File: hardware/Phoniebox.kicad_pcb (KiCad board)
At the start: 2 copper layers, 65 x 56.5 mm, 80 parts, among them J1 GPIO, J2 Screw_Terminal_01x08, J3 Screw_Terminal_01x08, J4 Screw_Terminal_01x08, J7 USB_B_Micro, J8 Conn_02x04_Odd_Even, Q1 2N7002, Q2 2N7002, Q3 2N7002, Q4 2N7002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

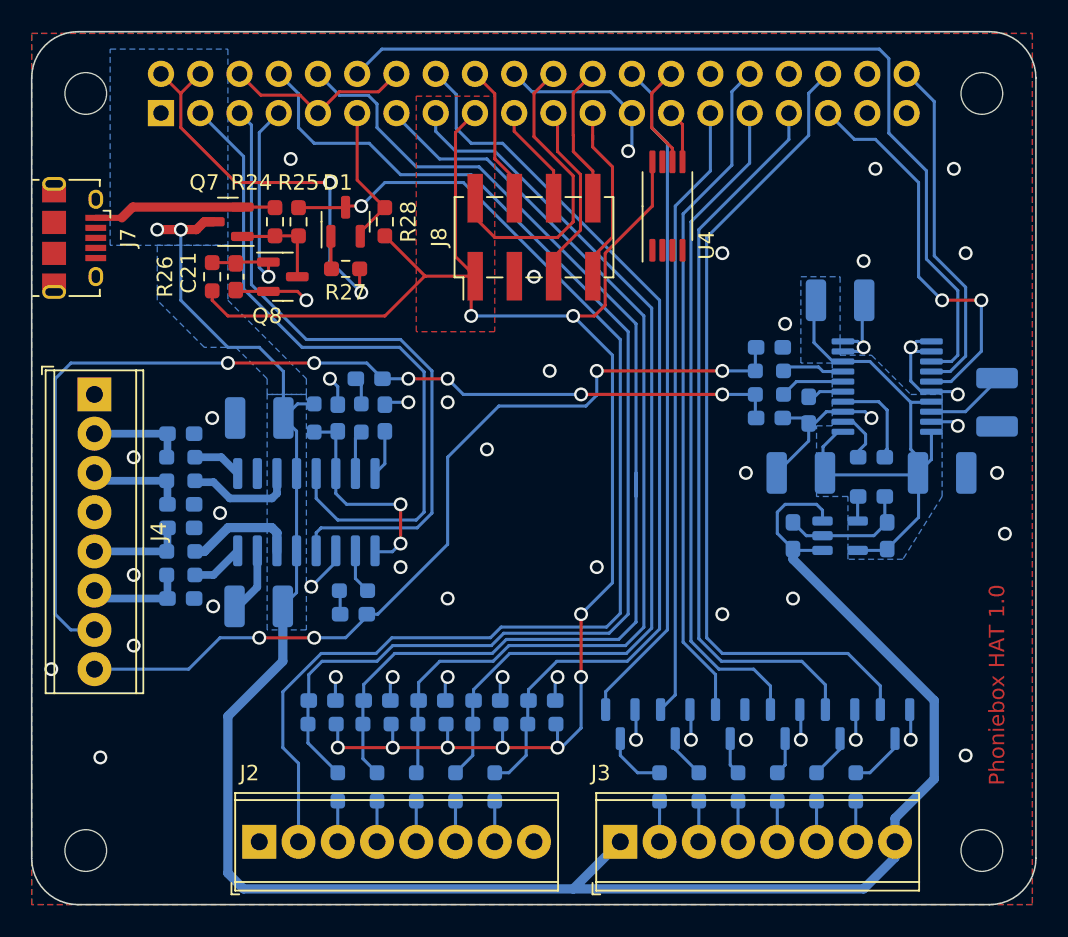
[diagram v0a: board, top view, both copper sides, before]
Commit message: Add I2C header for displays. Mute/SHDN now controlled by previously unused GPIO20/26. LED1 is now hardwired to ON=V3P3 high. GPIO7 would still be available to control LED1. Change debounce circuit to have both directions up/down debounced. Use resistor/capacitor values to debounce button press times <100ms.
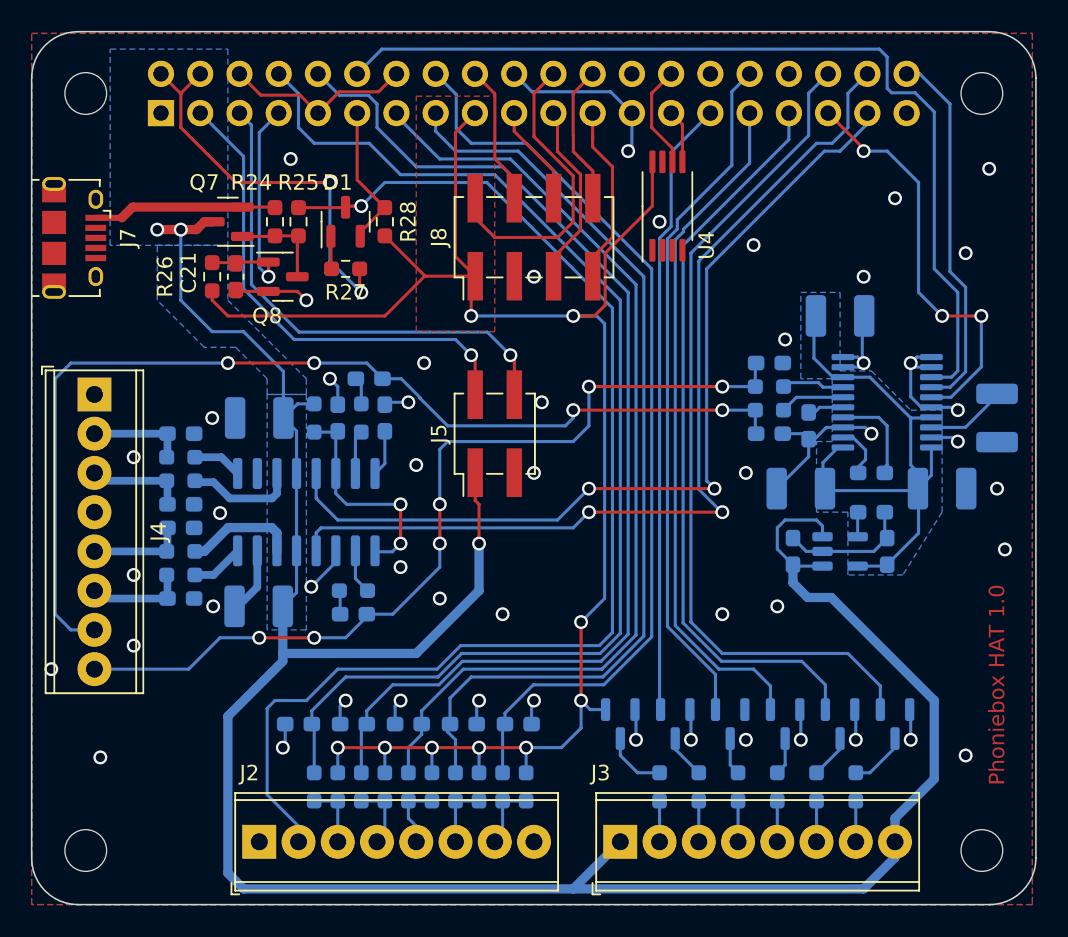
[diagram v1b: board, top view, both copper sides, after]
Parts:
- added J5: Conn_02x02_Odd_Even, Connector_PinHeader_2.54mm:PinHeader_2x02_P2.54mm_Vertical_SMD, F.Cu at (130.0, 69.5)
- C14, C15, C16, C8, C9: value 1n -> 1u
- R10, R12, R20, R6, R8: value 10k -> 33k
- R13, R21, R7, R9: value 100 -> 33k
- moved R20 4.19 mm to (132.0, 92.4), turned to 90 degrees
- moved R6 4.19 mm to (119.8, 92.4), turned to 90 degrees
- moved R12 4.10 mm to (129.0, 92.4), turned to 90 degrees
- moved R8 4.10 mm to (122.9, 92.4), turned to 90 degrees
- moved R10 4.06 mm to (125.9, 92.4), turned to 90 degrees
- moved C14 2.16 mm to (124.4, 88.3), turned to 180 degrees
- moved C15 2.16 mm to (127.9, 88.3)
- moved C16 2.16 mm to (131.5, 88.3)
- moved C8 2.16 mm to (117.3, 88.3), turned to 180 degrees
- moved C9 2.16 mm to (120.8, 88.3), turned to 180 degrees
- moved R7 1.52 mm to (118.3, 92.4)
- moved C17 1.02 mm to (149.3, 77.1)
- moved C22 1.02 mm to (155.4, 77.1)
- moved C24 1.02 mm to (154.4, 72.1)
- moved C25 1.02 mm to (150.3, 69.0)
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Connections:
- J1 pad 3: /GPIO2 -> /GPIO2_SDA
- J1 pad 37: /GPIO[26] -> /GPIO26
- J1 pad 38: /GPIO[20]/PCM.DIN -> /GPIO20
- J1 pad 5: /GPIO3 -> /GPIO3_SCL
- Q1 pad 1: /GPIO7 -> +3V3
- R10 pad 1: /GPIO27 -> /Button_4
- R12 pad 1: /GPIO22 -> /Button_5
- R20 pad 1: /GPIO23 -> /Button_6
- R6 pad 1: /GPIO14 -> /Button_2
- R8 pad 1: /GPIO15 -> /Button_3
- U1 pad 12: /GPIO3 -> /GPIO20
- U1 pad 5: /GPIO2 -> /GPIO26
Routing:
- net /GPIO20: track 0.00 -> 62.2 mm, vias 0 -> 2
- net /GPIO26: track 0.00 -> 58.2 mm, vias 0 -> 2
- net /GPIO2: track 44.9 -> 0.00 mm
- net /GPIO3: track 43.9 -> 0.00 mm
- net /GPIO7: track 43.8 -> 0.00 mm
- net /GPIO3_SCL: track 0.00 -> 32.7 mm, vias 0 -> 1
- net /GPIO2_SDA: track 0.00 -> 31.7 mm, vias 0 -> 1
- net +5V: track 162.8 -> 184.8 mm, vias 4 -> 5
- net +3V3: track 109.3 -> 111.9 mm
- net /GPIO15: track 74.4 -> 72.1 mm
- net /GPIO18: track 58.3 -> 60.2 mm
- net /Button_4: track 2.64 -> 4.38 mm
- net /Button_3: track 2.64 -> 4.38 mm
- net /Button_6: track 2.64 -> 4.38 mm
- net /Button_1: track 77.5 -> 79.2 mm
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
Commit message: Add BOM descriptions and JLC PCB LCSC part numbers. Generate gerber, drill and pick-and-place files.
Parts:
- C24, C25: value 2u2 -> 4u7
- U4: value CAT24C128 -> CAT24C32

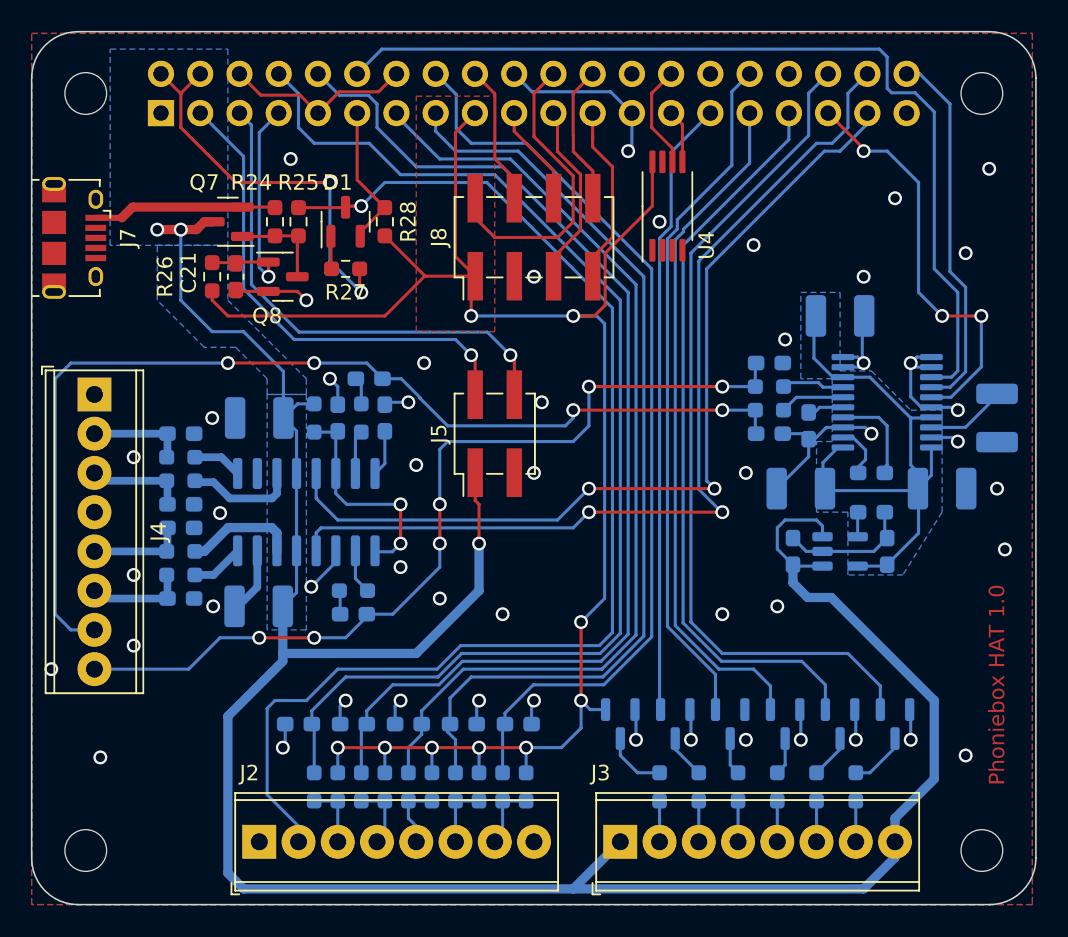
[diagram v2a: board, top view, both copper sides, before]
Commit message: Place on/off SHIM and EEPROM on bot
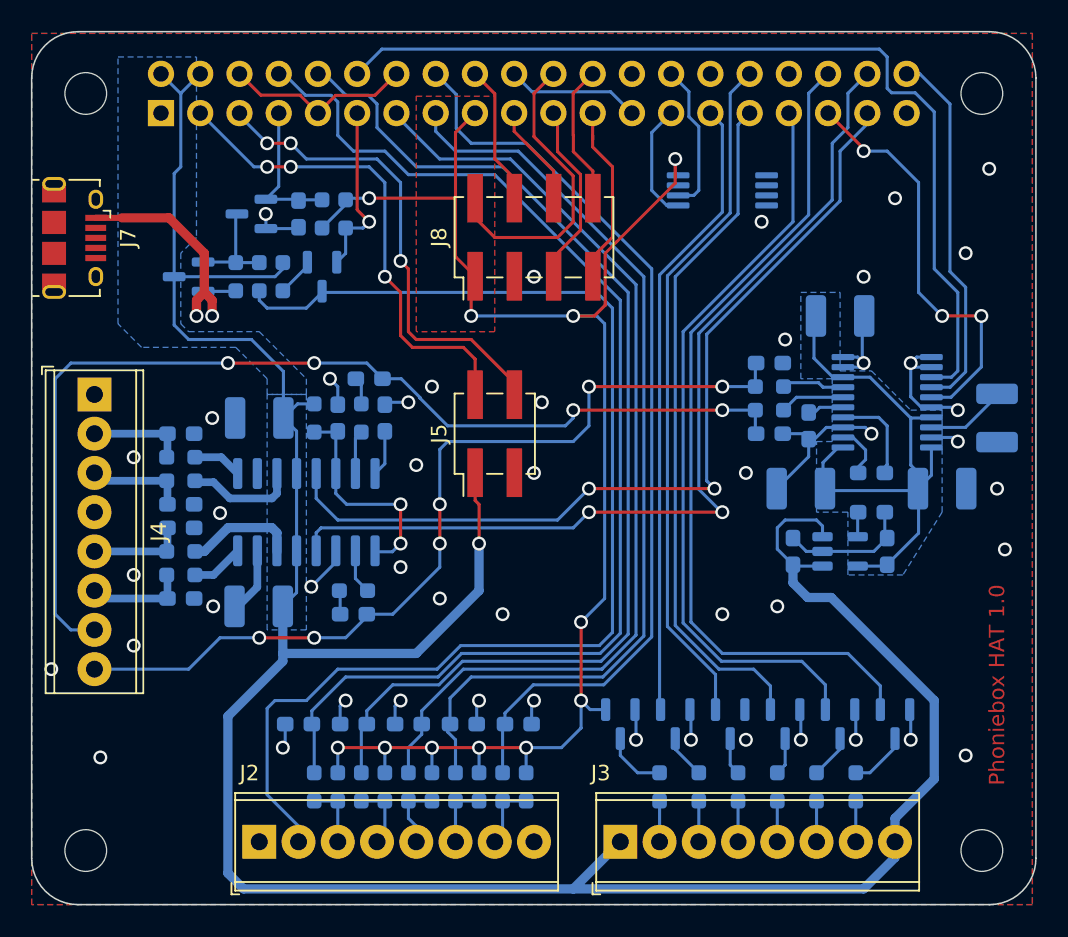
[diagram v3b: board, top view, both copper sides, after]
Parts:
- C21, D1, Q7, Q8, R24, R25, R26, R27, R28, U4: moved to B.Cu
- moved R26 8.19 mm to (118.8, 55.3)
- moved C21 5.75 mm to (117.3, 55.3)
- moved Q8 4.54 mm to (114.2, 55.3), turned to 180 degrees
- moved Q7 4.37 mm to (110.2, 59.4)
- moved R24 4.37 mm to (113.2, 59.4), turned to -90 degrees
- moved R25 4.37 mm to (114.7, 59.4), turned to 90 degrees
- moved R27 4.10 mm to (116.3, 59.4), turned to 90 degrees
- moved D1 3.87 mm to (118.8, 59.4), turned to -90 degrees
- moved U4 3.70 mm to (144.7, 53.8), turned to 180 degrees
- moved R28 2.59 mm to (120.3, 55.3), turned to 90 degrees
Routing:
- net +3V3: track 111.9 -> 100.6 mm, vias 9 -> 11
- net +5V: track 184.8 -> 176.1 mm, vias 5 -> 1
- net /OnOffSHIM/VBUS: track 11.9 -> 19.7 mm, vias 0 -> 2
- net /GPIO4_PowerOff: track 16.0 -> 9.61 mm, vias 1 -> 0
- net GND: track 92.6 -> 88.3 mm, vias 51 -> 48
- net /ID_SDA: track 3.46 -> 7.64 mm
- net /ID_SCL: track 6.77 -> 9.76 mm
- net /GPIO17_Trigger: track 9.37 -> 11.5 mm, vias 0 -> 1
- net /GPIO3_SCL: track 32.7 -> 31.2 mm, vias 1 -> 3
- net /GPIO5: track 40.0 -> 40.6 mm
- net /GPIO26: track 58.2 -> 57.6 mm
- net /GPIO20: track 62.2 -> 61.6 mm
- net /OnOffSHIM/Q7_G: track 6.33 -> 6.83 mm
- net /Button_1: track 79.2 -> 79.5 mm, vias 1 -> 0
- net /GPIO2_SDA: track 31.7 -> 31.9 mm, vias 1 -> 3

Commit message: Replace micro USB connector with USB-C type connector. DRC errors exist.
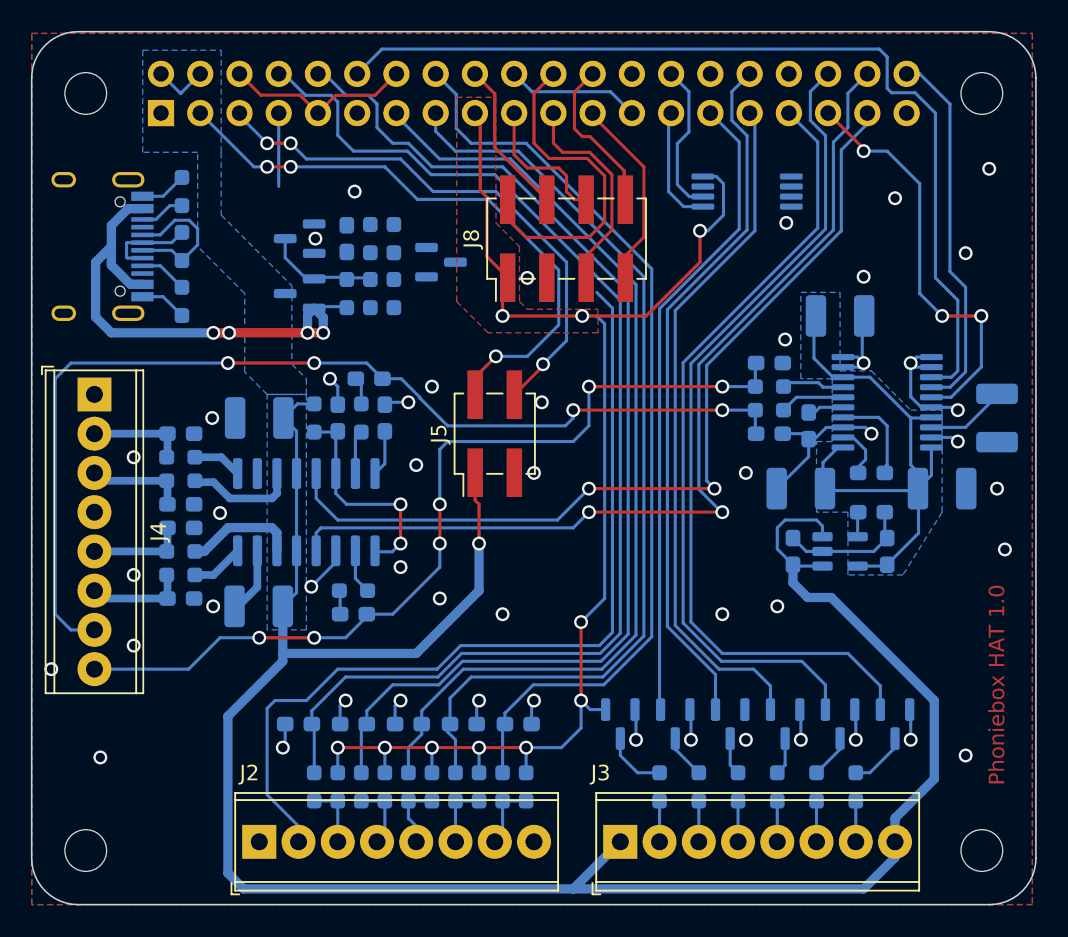
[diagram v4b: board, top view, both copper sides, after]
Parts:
- added R1: 10, Resistor_SMD:R_0603_1608Metric_Pad0.98x0.95mm_HandSolder, B.Cu at (109.7, 57.4)
- added R2: 5k11, Resistor_SMD:R_0603_1608Metric_Pad0.98x0.95mm_HandSolder, B.Cu at (109.7, 53.8)
- added R30: 5k11, Resistor_SMD:R_0603_1608Metric_Pad0.98x0.95mm_HandSolder, B.Cu at (109.7, 61.0)
- J7: value USB_B_Micro -> USB_C_Receptacle_USB2.0; footprint Connector_USB:USB_Micro-B_Amphenol_10118194_Horizontal -> Connector_USB:USB_C_Receptacle_HRO_TYPE-C-31-M-12; moved to B.Cu
- moved D1 7.75 mm to (126.5, 58.4), turned to 0 degrees
- moved Q7 7.27 mm to (117.3, 60.5)
- moved R24 7.27 mm to (120.4, 60.5)
- moved R25 7.27 mm to (121.9, 60.5)
- moved R27 7.27 mm to (123.4, 60.5)
- moved R28 3.51 mm to (123.4, 56.9), turned to -90 degrees
- moved C21 3.51 mm to (120.4, 56.9)
- moved Q8 3.51 mm to (117.3, 56.9)
- moved R26 3.51 mm to (121.9, 56.9)
- moved J8 2.11 mm to (134.6, 56.9)
- moved U4 1.60 mm to (146.3, 53.8)
- moved J7 0.67 mm to (103.1, 57.4), turned to 90 degrees
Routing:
- net +5V: track 176.1 -> 142.0 mm
- net /Button_1: track 79.5 -> 56.3 mm
- net /OnOffSHIM/VBUS: track 19.7 -> 34.5 mm, vias 2 -> 4
- net /GPIO17_Trigger: track 11.5 -> 0.00 mm, vias 1 -> 0
- net +3V3: track 100.6 -> 90.7 mm, vias 11 -> 10
- net Net-(J7-PadA6): track 0.00 -> 9.51 mm
- net /GPIO2_SDA: track 31.9 -> 38.9 mm, vias 3 -> 4
- net Net-(J7-PadA7): track 0.00 -> 5.82 mm
- net /GPIO4_PowerOff: track 9.61 -> 4.75 mm
- net /GPIO3_SCL: track 31.2 -> 36.0 mm
- net Net-(J7-PadA5): track 0.00 -> 3.14 mm
- net GND: track 88.3 -> 91.3 mm
- net Net-(J7-PadB5): track 0.00 -> 2.93 mm
- net /MOSI: track 6.57 -> 9.16 mm
- net Net-(D1-Pad1): track 2.51 -> 0.00 mm
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
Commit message: Fixed gridd issues. Properly added USB-C connector. Fixed DRC errors.
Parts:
- moved J7 1.02 mm to (104.1, 57.4)
- moved R1 1.02 mm to (110.7, 57.4)
- moved R2 1.02 mm to (110.7, 53.8)
- moved R30 1.02 mm to (110.7, 61.0)
- moved C18 0.11 mm to (149.9, 73.2)
- moved R12 0.11 mm to (129.0, 92.5)
- moved R14 0.11 mm to (140.7, 92.5)
- moved R17 0.11 mm to (148.3, 92.5)
- moved R20 0.11 mm to (132.1, 92.5)
- moved R21 0.11 mm to (130.6, 92.5)
- moved C2 0.11 mm to (121.9, 66.0)
- moved Q5 0.11 mm to (145.3, 88.4)
- moved R6 0.11 mm to (119.9, 92.5)
- moved R7 0.11 mm to (118.4, 92.5)
- moved R8 0.11 mm to (122.9, 92.5)
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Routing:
- net +5V: track 142.0 -> 174.5 mm
- net /Button_1: track 56.3 -> 81.6 mm, vias 0 -> 2
- net GND: track 91.3 -> 104.2 mm, vias 48 -> 54
- net /GPIO17_Trigger: track 0.00 -> 11.2 mm, vias 0 -> 1
- net +3V3: track 90.7 -> 98.4 mm
- net /GPIO4_PowerOff: track 4.75 -> 12.2 mm, vias 0 -> 1
- net /GPIO2_SDA: track 38.9 -> 34.3 mm, vias 4 -> 1
- net /GPIO3_SCL: track 36.0 -> 32.4 mm, vias 3 -> 1
- net Net-(D1-Pad1): track 0.00 -> 2.94 mm
- net /OnOffSHIM/VBUS: track 34.5 -> 36.1 mm
- net /IRQ: track 11.4 -> 10.1 mm
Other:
- board text added: "Buttons"
- board text added: "I2C"
- board text added: "LEDs"
- board text added: "RC522"
- board text added: "Speaker"
- board text added: "Supply"
